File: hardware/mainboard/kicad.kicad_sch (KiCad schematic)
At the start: 22 parts, among them J1 Screw_Terminal_01x02, J2 Screw_Terminal_01x03, J3 Screw_Terminal_01x03, J4 Screw_Terminal_01x03, J5 Conn_01x03, J6 ICSP, J7 Conn_01x05, SW1 SW_Push, SW2 SW_Push, U1 DS1233A-10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

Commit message: add relay expansion pcb
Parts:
- removed J7: Conn_01x05, Connector_Molex:Molex_KK-254_AE-6410-05A_1x05_P2.54mm_Vertical, symbol Connector_Generic:Conn_01x05
- added J?: Conn_01x06, Connector_Molex:Molex_KK-254_AE-6410-06A_1x06_P2.54mm_Vertical, symbol Connector_Generic:Conn_01x06
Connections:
- net +3V3: now also J?.4 (Pin_4)
- net +5V: now also J?.5 (Pin_5)
- net GND: now also J?.6 (Pin_6)
- net SCL: now also J?.2 (Pin_2)
- net SDA: now also J?.3 (Pin_3)
- new net INT: J?.1 (Pin_1)
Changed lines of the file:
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@@
+    (stroke (width 0) (type default) (color 0 0 0 0))
+  )
+  (wire (pts (xy 99.06 184.15) (xy 120.65 184.15))
+    (stroke (width 0) (type default) (color 0 0 0 0))
+  )
+  (wire (pts (xy 120.65 184.15) (xy 120.65 173.99))
     (stroke (width 0) (type default) (color 0 0 0 0))
   )
@@
   )
   (wire (pts (xy 208.28 69.85) (xy 212.09 69.85))
+    (stroke (width 0) (type default) (color 0 0 0 0))
+  )
+  (wire (pts (xy 120.65 173.99) (xy 124.46 173.99))
     (stroke (width 0) (type default) (color 0 0 0 0))
   )
@@
     )
   )
+  (global_label "INT" (shape input) (at 99.06 184.15 180) (fields_autoplaced)
+    (effects (font (size 0.9906 0.9906)) (justify right))
+    (property "Intersheet References" "${INTERSHEET_REFS}" (id 0) (at 94.9137 184.0881 0)
+      (effects (font (size 0.9906 0.9906)) (justify right) hide)
+    )
+  )
   (global_label "GPIO0" (shape output) (at 184.15 49.53 0) (fields_autoplaced)
     (effects (font (size 0.9906 0.9906)) (justify left))
@@
     )
     (pin "1")
-  )
-  (symbol (lib_id "Connector_Generic:Conn_01x05") (at 129.54 181.61 0) (unit 1)
-    (in_bom yes) (on_board yes)
-    (property "Reference" "J7" (id 0) (at 125.73 172.72 0)
-      (effects (font (size 1.27 1.27)) (justify left))
-    )
-    (property "Value" "Conn_01x05" (id 1) (at 131.572 182.8546 0)
-      (effects (font (size 1.27 1.27)) (justify left) hide)
-    )
-    (property "Footprint" "Connector_Molex:Molex_KK-254_AE-6410-05A_1x05_P2.54mm_Vertical" (id 2) (at 129.54 181.61 0)
-      (effects (font (size 1.27 1.27)) hide)
-    )
-    (property "Datasheet" "https://app.adam-tech.com/products/download/data_sheet/196588/lha-xx-ts-data-sheet.pdf" (id 3) (at 129.54 181.61 0)
-      (effects (font (size 1.27 1.27)) hide)
-    )
-    (property "manf#" "LHA-05-TS" (id 4) (at 129.54 181.61 0)
-      (effects (font (size 1.27 1.27)) hide)
-    )
-    (pin "1")
-    (pin "2")
-    (pin "3")
-    (pin "4")
-    (pin "5")
   )
   (symbol (lib_id "power:+5V") (at 123.19 165.1 0) (unit 1)
@@
     (pin "6")
   )
+  (symbol (lib_id "Connector_Generic:Conn_01x06") (at 129.54 179.07 0) (unit 1)
+    (in_bom yes) (on_board yes)
+    (property "Reference" "J?" (id 0) (at 125.73 170.18 0)
+      (effects (font (size 1.27 1.27)) (justify left))
+    )
+    (property "Value" "Conn_01x06" (id 1) (at 132.08 181.6099 0)
+      (effects (font (size 1.27 1.27)) (justify left) hide)
+    )
+    (property "Footprint" "Connector_Molex:Molex_KK-254_AE-6410-06A_1x06_P2.54mm_Vertical" (id 2) (at 129.54 179.07 0)
+      (effects (font (size 1.27 1.27)) hide)
+    )
+    (property "Datasheet" "~" (id 3) (at 129.54 179.07 0)
+      (effects (font (size 1.27 1.27)) hide)
+    )
+    (pin "1")
+    (pin "2")
+    (pin "3")
+    (pin "4")
+    (pin "5")
+    (pin "6")
+  )
   (symbol (lib_id "power:+3V3") (at 180.34 39.37 0) (unit 1)
     (in_bom yes) (on_board yes)
@@
       (reference "J6") (unit 1) (value "ICSP") (footprint "Connector_PinSocket_2.54mm:PinSocket_1x06_P2.54mm_Vertical")
     )
-    (path "/00000000-0000-0000-0000-000060c734c6"
-      (reference "J7") (unit 1) (value "Conn_01x05") (footprint "Connector_Molex:Molex_KK-254_AE-6410-05A_1x05_P2.54mm_Vertical")
-    )
     (path "/00000000-0000-0000-0000-0000612f4d6e/00000000-0000-0000-0000-000061313c16"
       (reference "J8") (unit 1) (value "Conn_01x03") (footprint "Connector_Molex:Molex_KK-254_AE-6410-03A_1x03_P2.54mm_Vertical")
@@
       (reference "J11") (unit 1) (value "Conn_01x06") (footprint "Connector_Molex:Molex_KK-254_AE-6410-06A_1x06_P2.54mm_Vertical")
     )
+    (path "/aaf01c9a-c9a3-4e42-a983-ec360a40fbc7"
+      (reference "J?") (unit 1) (value "Conn_01x06") (footprint "Connector_Molex:Molex_KK-254_AE-6410-06A_1x06_P2.54mm_Vertical")
+    )
     (path "/00000000-0000-0000-0000-00006121a9ea/00000000-0000-0000-0000-0000612af526"

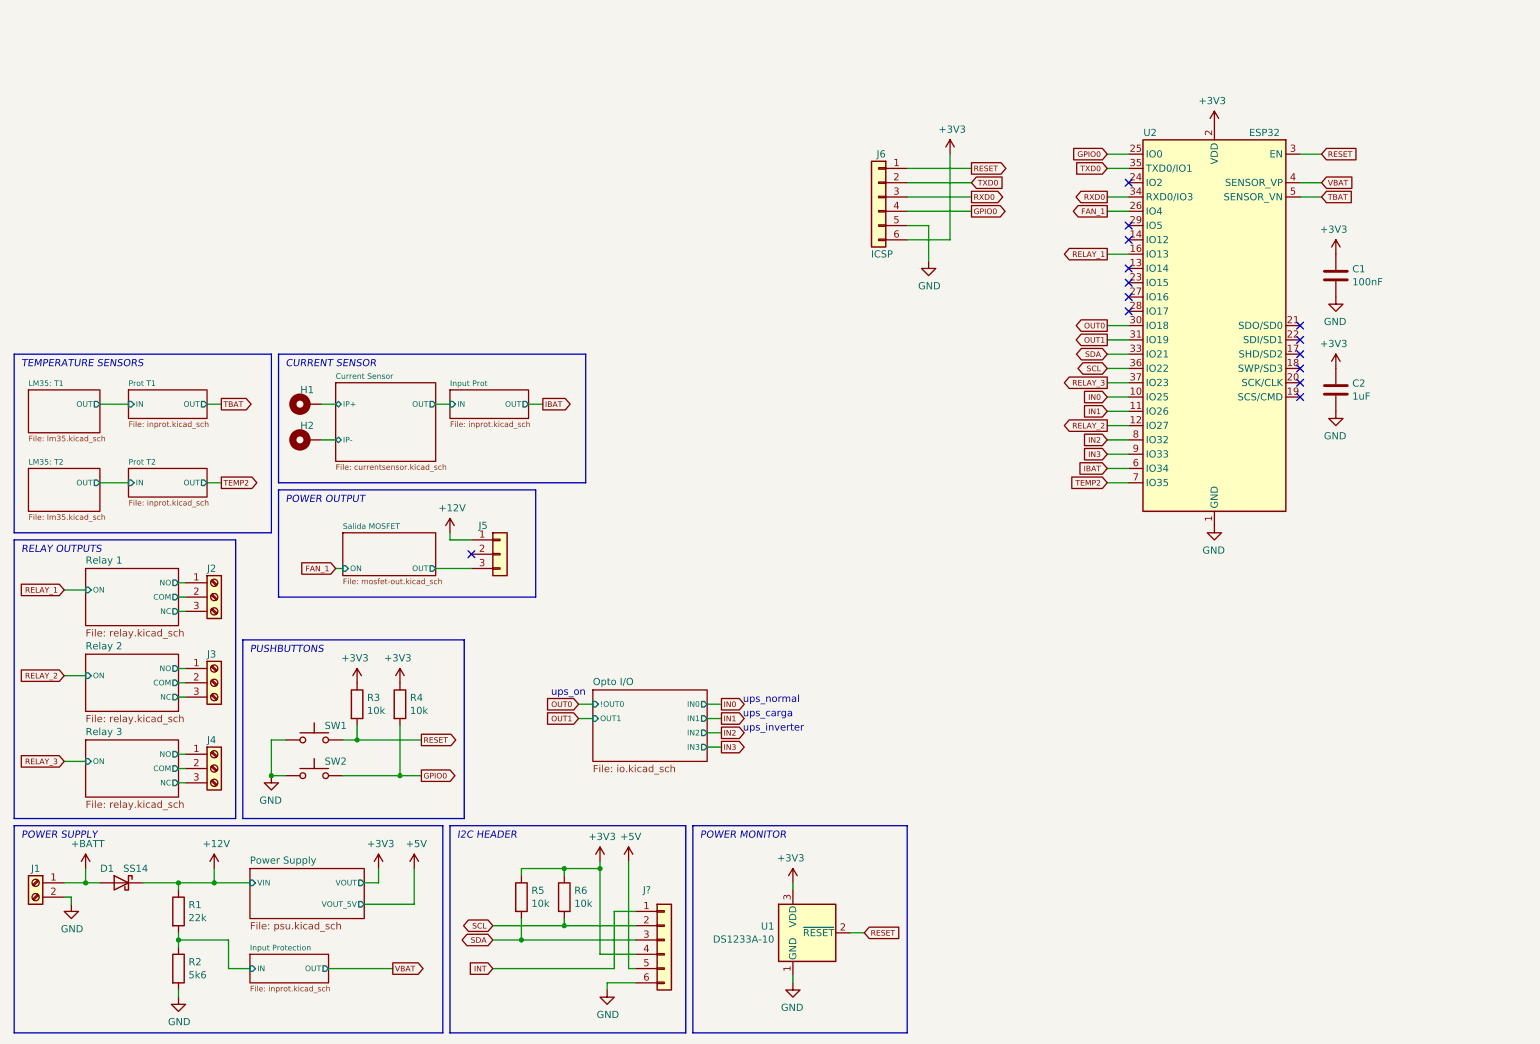
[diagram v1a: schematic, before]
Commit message: Diseños casi listos (sch)
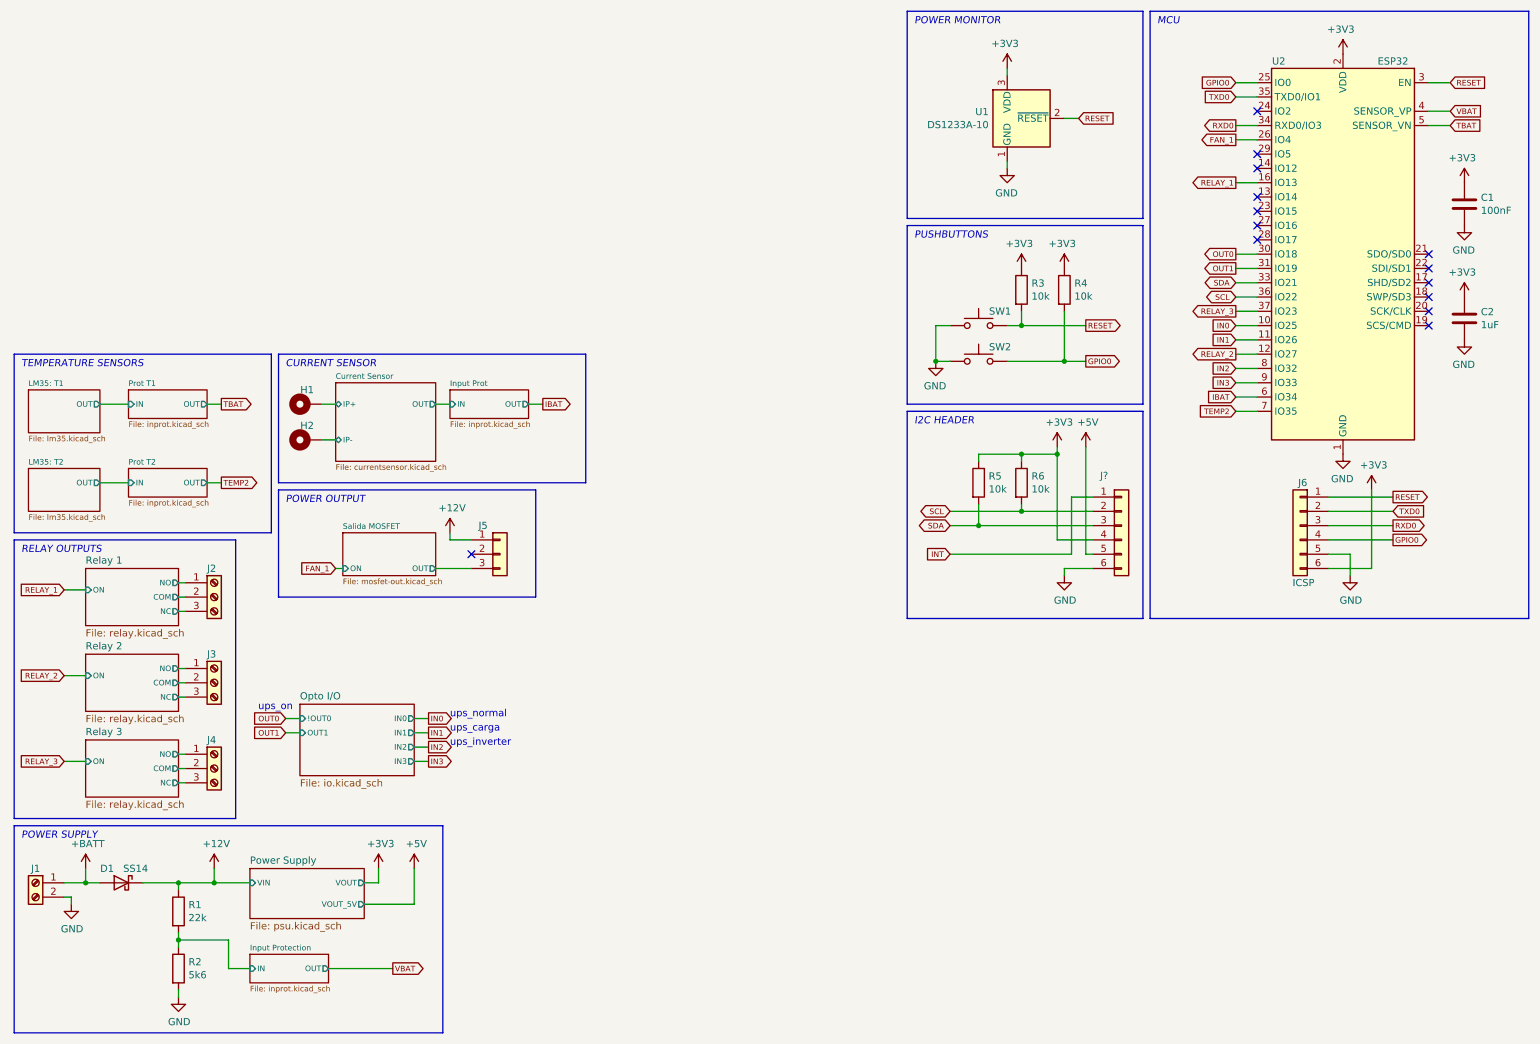
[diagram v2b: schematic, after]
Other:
- note added: "MCU"
- moved on the sheet: C1, C2, J6, J?, R3, R4, R5, R6, SW1, SW2, U1, U2

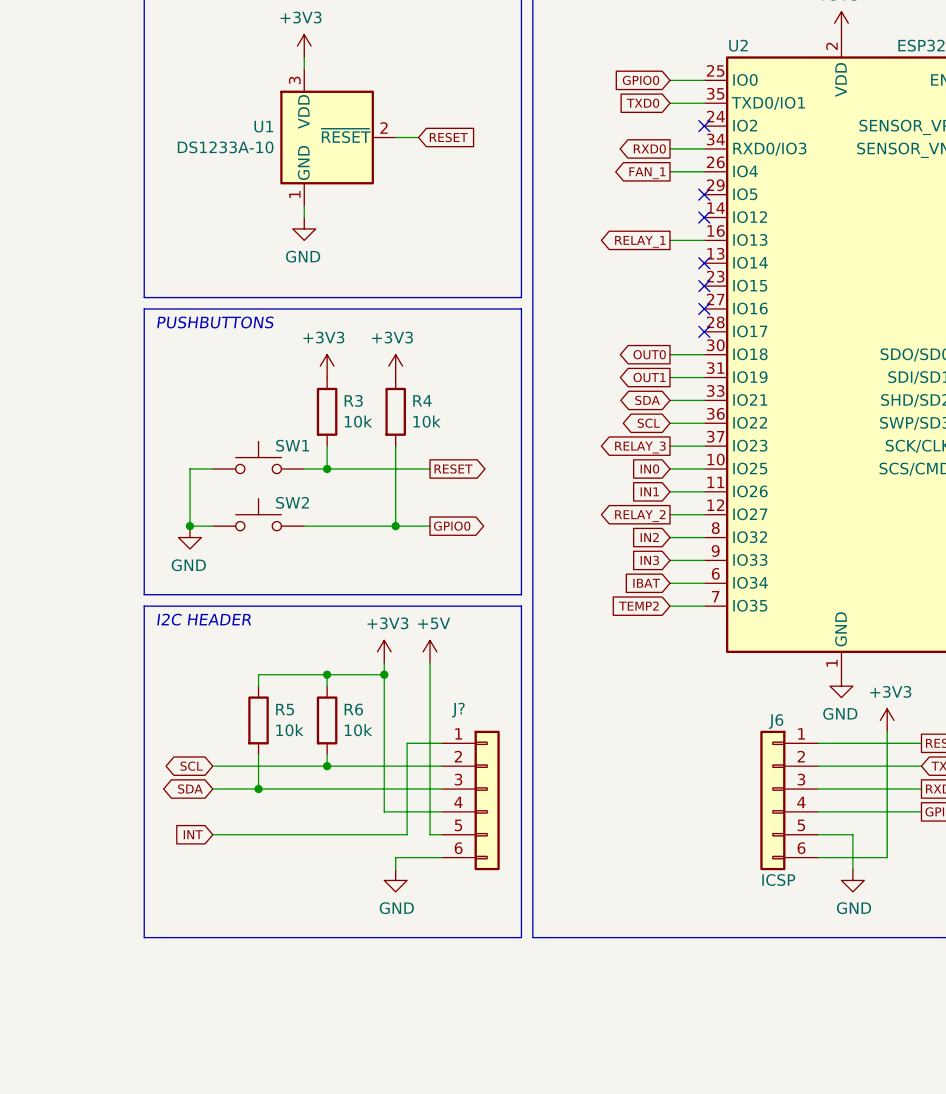
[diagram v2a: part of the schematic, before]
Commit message: Mainboard routeado.
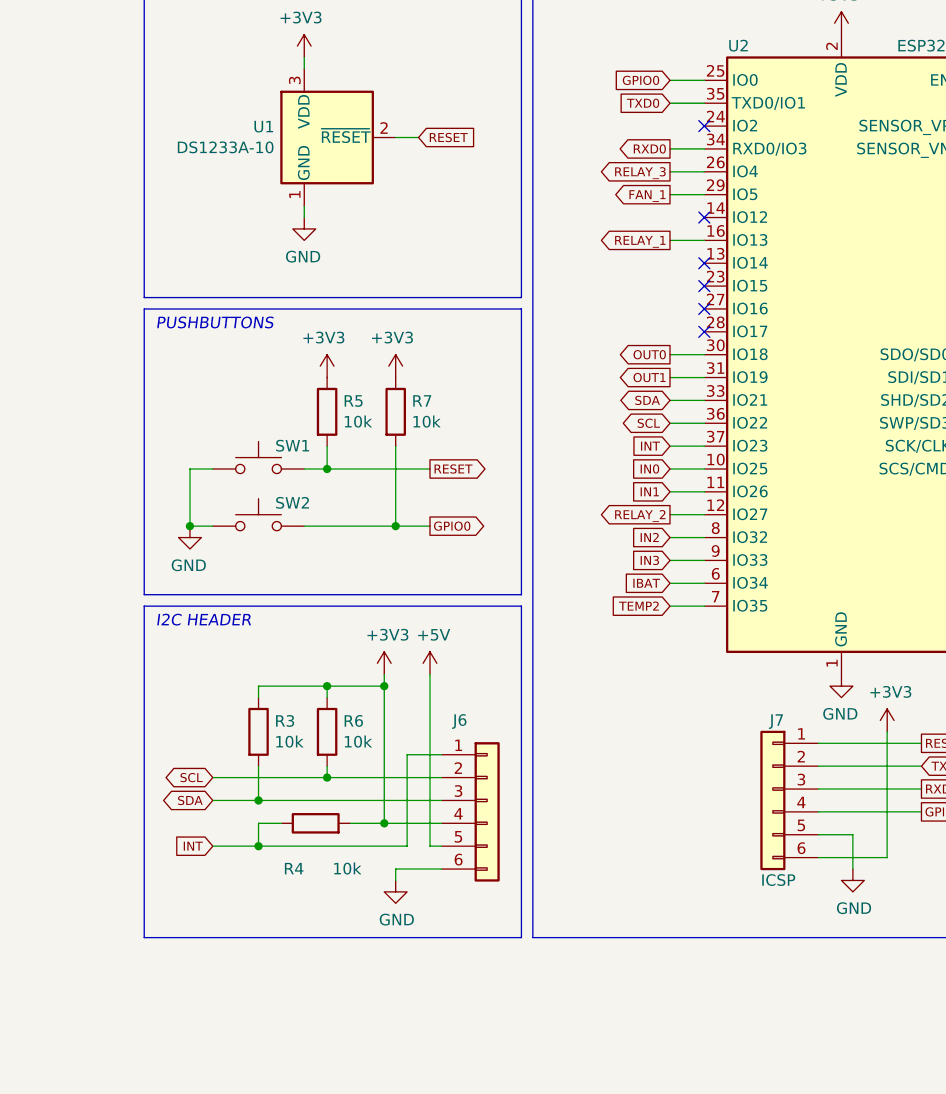
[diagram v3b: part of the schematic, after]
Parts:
- removed J?: Conn_01x06, Connector_Molex:Molex_KK-254_AE-6410-06A_1x06_P2.54mm_Vertical, symbol Connector_Generic:Conn_01x06
- removed R5: 10k, Resistor_SMD:R_1206_3216Metric, symbol Device:R
- added J6: Conn_01x06, Connector_Molex:Molex_KK-254_AE-6410-06A_1x06_P2.54mm_Vertical, symbol Connector_Generic:Conn_01x06
- added R3, R4: 10k, Resistor_SMD:R_1206_3216Metric, symbol Device:R
- R6: Fitted (none) -> Yes
- renumbered J6 to J7, R3 to R5, R4 to R7
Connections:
- net +3V3: now also J6.4 (Pin_4), R3.1, R4.2
- net +5V: now also J6.5 (Pin_5)
- net FAN_1: now also U2.29 (IO5); no longer U2.26 (IO4)
- net GND: now also J6.6 (Pin_6)
- net INT: now also U2.37 (IO23), J6.1 (Pin_1), R4.1
- net RELAY_3: now also U2.26 (IO4); no longer U2.37 (IO23)
- net SCL: now also J6.2 (Pin_2)
- net SDA: now also J6.3 (Pin_3), R3.2
- no-connect marks 14 -> 13
